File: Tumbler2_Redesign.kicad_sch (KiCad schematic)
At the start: 0 parts

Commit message: Add ESP32 and USB
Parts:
- added J1: USB_C_Receptacle_USB2.0_16P, symbol Connector:USB_C_Receptacle_USB2.0_16P
- added U1: ESP32-S3-WROOM-1, RF_Module:ESP32-S3-WROOM-1, symbol RF_Module:ESP32-S3-WROOM-1
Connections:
- new net: U1.1 (GND), U1.40 (GND), U1.41 (GND)
- new net: J1.A1 (GND), J1.A12 (GND), J1.B1 (GND), J1.B12 (GND)
- new net: J1.A4 (VBUS), J1.A9 (VBUS), J1.B4 (VBUS), J1.B9 (VBUS)
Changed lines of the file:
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@@
 	(generator_version "9.0")
 	(paper "A4")
+	(symbol
+		(lib_id "RF_Module:ESP32-S3-WROOM-1")
+		(at 142.24 86.36 0)
+		(unit 1)
+		(exclude_from_sim no)
+		(in_bom yes)
+		(on_board yes)
+		(dnp no)
+		(fields_autoplaced yes)
+		(property "Reference" "U1"
+			(at 144.3833 55.88 0)
+			(effects
+				(font
+					(size 1.27 1.27)
+				)
+				(justify left)
+			)
+		)
+		(property "Value" "ESP32-S3-WROOM-1"
+			(at 144.3833 58.42 0)
+			(effects
+				(font
+					(size 1.27 1.27)
+				)
+				(justify left)
+			)
+		)
+		(property "Footprint" "RF_Module:ESP32-S3-WROOM-1"
+			(at 142.24 83.82 0)
+			(effects
+				(font
+					(size 1.27 1.27)
+				)
+				(hide yes)
+			)
+		)
+		(property "Datasheet" "https://www.espressif.com/sites/default/files/documentation/esp32-s3-wroom-1_wroom-1u_datasheet_en.pdf"
+			(at 142.24 86.36 0)
+			(effects
+				(font
+					(size 1.27 1.27)
+				)
+				(hide yes)
+			)
+		)
+		(property "Description" "RF Module, ESP32-S3 SoC, Wi-Fi 802.11b/g/n, Bluetooth, BLE, 32-bit, 3.3V, onboard antenna, SMD"
+			(at 142.24 86.36 0)
+			(effects
+				(font
+					(size 1.27 1.27)
+				)
+				(hide yes)
+			)
+		)
+		(pin "12"
+		)
+		(pin "40"
+		)
+		(pin "20"
+		)
+		(pin "18"
+		)
+		(pin "15"
+		)
+		(pin "13"
+		)
+		(pin "23"
+		)
+		(pin "29"
+		)
+		(pin "31"
+		)
+		(pin "39"
+		)
+		(pin "3"
+		)
+		(pin "5"
+		)
+		(pin "17"
+		)
+		(pin "38"
+		)
+		(pin "19"
+		)
+		(pin "37"
+		)
+		(pin "27"
+		)
+		(pin "6"
+		)
+		(pin "8"
+		)
+		(pin "4"
+		)
+		(pin "7"
+		)
+		(pin "9"
+		)
+		(pin "2"
+		)
+		(pin "1"
+		)
+		(pin "22"
+		)
+		(pin "21"
+		)
+		(pin "41"
+		)
+		(pin "36"
+		)
+		(pin "10"
+		)
+		(pin "11"
+		)
+		(pin "14"
+		)
+		(pin "28"
+		)
+		(pin "30"
+		)
+		(pin "24"
+		)
+		(pin "33"
+		)
+		(pin "16"
+		)
+		(pin "26"
+		)
+		(pin "34"
+		)
+		(pin "25"
+		)
+		(pin "32"
+		)
+		(pin "35"
+		)
+		(instances
+			(project ""
+				(path "/f3fd8d79-9d35-4c04-811e-2697a2740958"
+					(reference "U1")
+					(unit 1)
+				)
+			)
+		)
+	)
+	(symbol
+		(lib_id "Connector:USB_C_Receptacle_USB2.0_16P")
+		(at 207.01 111.76 0)
+		(unit 1)
+		(exclude_from_sim no)
+		(in_bom yes)
+		(on_board yes)
+		(dnp no)
+		(fields_autoplaced yes)
+		(property "Reference" "J1"
+			(at 207.01 88.9 0)
+			(effects
+				(font
+					(size 1.27 1.27)
+				)
+			)
+		)
+		(property "Value" "USB_C_Receptacle_USB2.0_16P"
+			(at 207.01 91.44 0)
+			(effects
+				(font
+					(size 1.27 1.27)
+				)
+			)
+		)
+		(property "Footprint" ""
+			(at 210.82 111.76 0)
+			(effects
+				(font
+					(size 1.27 1.27)
+				)
+				(hide yes)
+			)
+		)
+		(property "Datasheet" "https://www.usb.org/sites/default/files/documents/usb_type-c.zip"
+			(at 210.82 111.76 0)
+			(effects
+				(font
+					(size 1.27 1.27)
+				)
+				(hide yes)
+			)
+		)
+		(property "Description" "USB 2.0-only 16P Type-C Receptacle connector"
+			(at 207.01 111.76 0)
+			(effects
+				(font
+					(size 1.27 1.27)
+				)
+				(hide yes)
+			)
+		)
+		(pin "S1"
+		)
+		(pin "B12"
+		)
+		(pin "B4"
+		)
+		(pin "A5"
+		)
+		(pin "A1"
+		)
+		(pin "A12"
+		)
+		(pin "B1"
+		)
+		(pin "A4"
+		)
+		(pin "A9"
+		)
+		(pin "B9"
+		)
+		(pin "B5"
+		)
+		(pin "B8"
+		)
+		(pin "A7"
+		)
+		(pin "B6"
+		)
+		(pin "B7"
+		)
+		(pin "A8"
+		)
+		(pin "A6"
+		)
+		(instances
+			(project ""
+				(path "/f3fd8d79-9d35-4c04-811e-2697a2740958"
+					(reference "J1")
+					(unit 1)
+				)
+			)
+		)
+	)
 	(sheet_instances
 		(path "/"

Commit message: Add further parts
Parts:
- added C1, C2, C3: C, symbol Device:C
- added D1: LED, symbol Device:LED
- added D2, D3, D4, D5: WS2812B, LED_SMD:LED_WS2812B-2020_PLCC4_2.0x2.0mm, symbol LED:WS2812B-2020
- added J2, J3: Conn_01x06, symbol Connector_Generic:Conn_01x06
- added J4, J5: Conn_01x04, symbol Connector_Generic:Conn_01x04
- added R1, R4, R5: R, symbol Device:R
- added R2, R3: 5k, symbol Device:R
- added SW1, SW2, SW3: SW_Push, symbol Switch:SW_Push
- added U2: USBLC6-2SC6, Package_TO_SOT_SMD:SOT-23-6, symbol Power_Protection:USBLC6-2SC6
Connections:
- net VBUS: now reaches J1.A4 (VBUS), J1.A9 (VBUS), J1.B4 (VBUS), J1.B9 (VBUS)
- net VBUS: now also U2.5 (VBUS)
- net at J1.A5 (CC1): now also R2.1
- net at J1.A6 (D+): now also J1.B6 (D+), U2.3 (I/O2)
- net at J1.A7 (D-): now also J1.B7 (D-), U2.1 (I/O1)
- net at J1.B5 (CC2): now also R3.1
- new net: D3.1 (DOUT), D4.3 (DIN)
- new net: D2.1 (DOUT), D3.3 (DIN)
- new net: D1.2 (A), R1.2
- new net: D4.1 (DOUT), D5.3 (DIN)
- new net GND: U2.2 (GND)

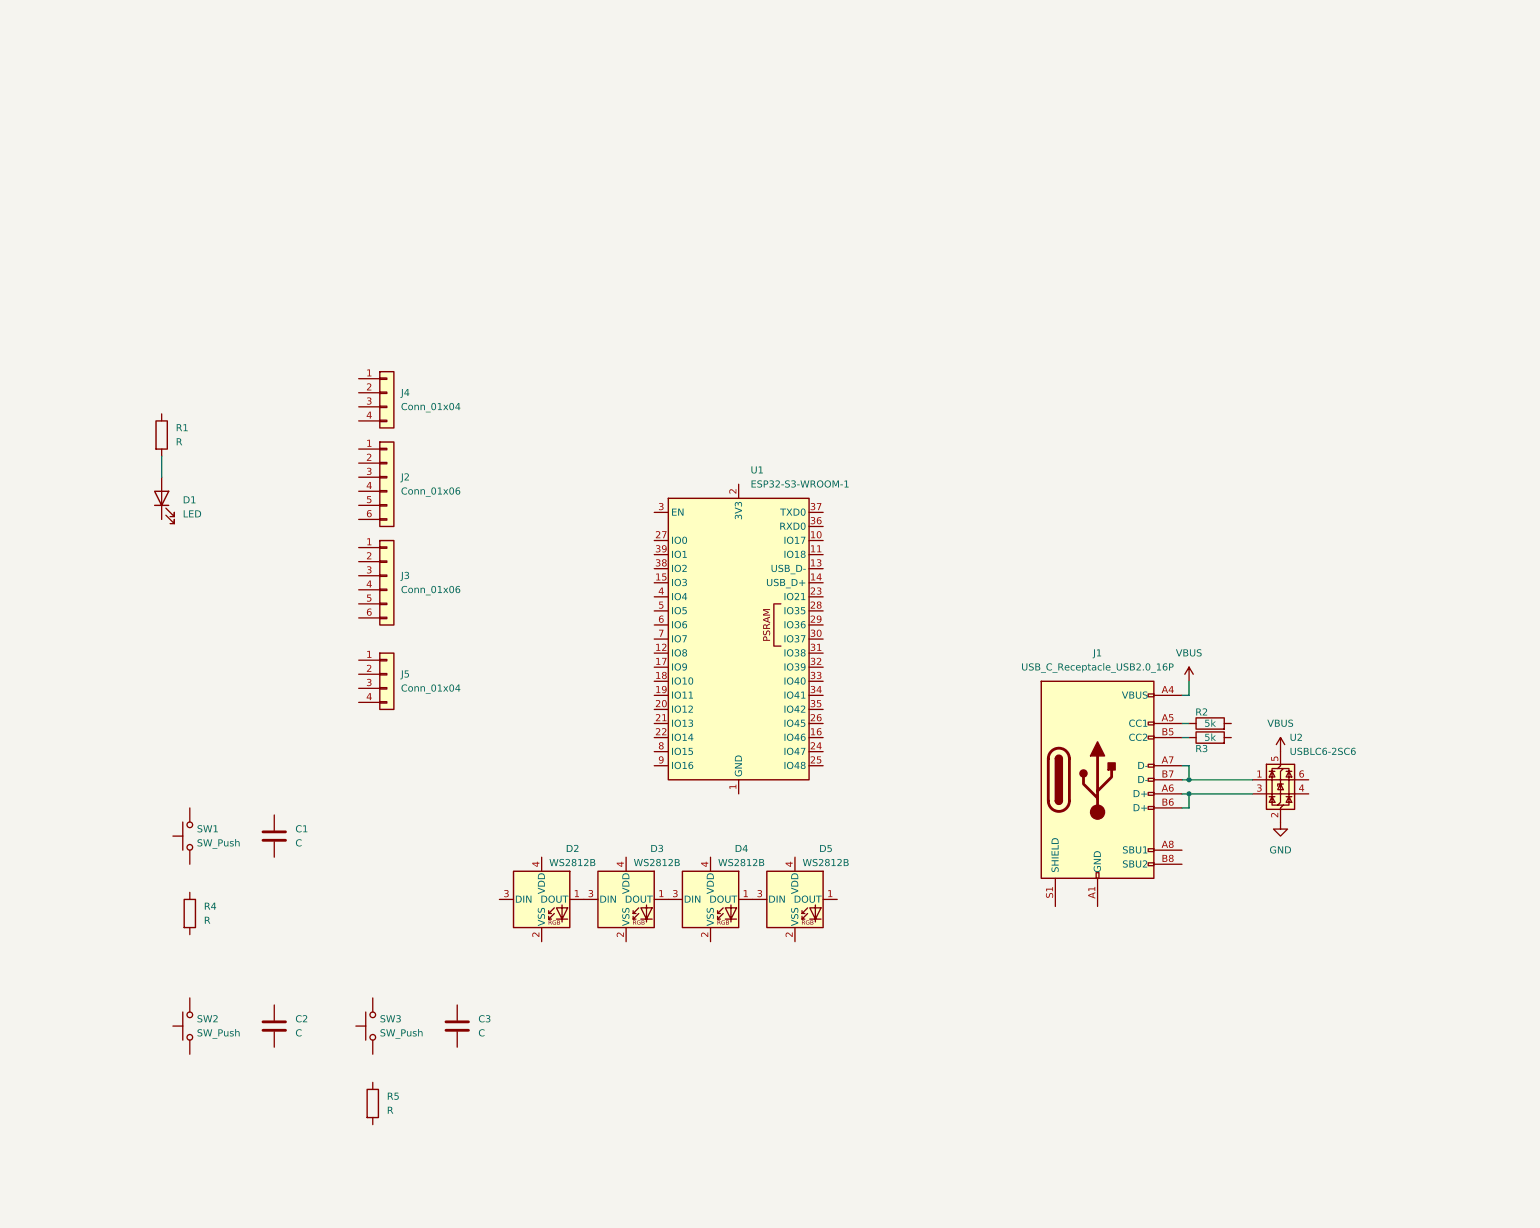
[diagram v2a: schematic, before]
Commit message: Add regulators and USB to UART
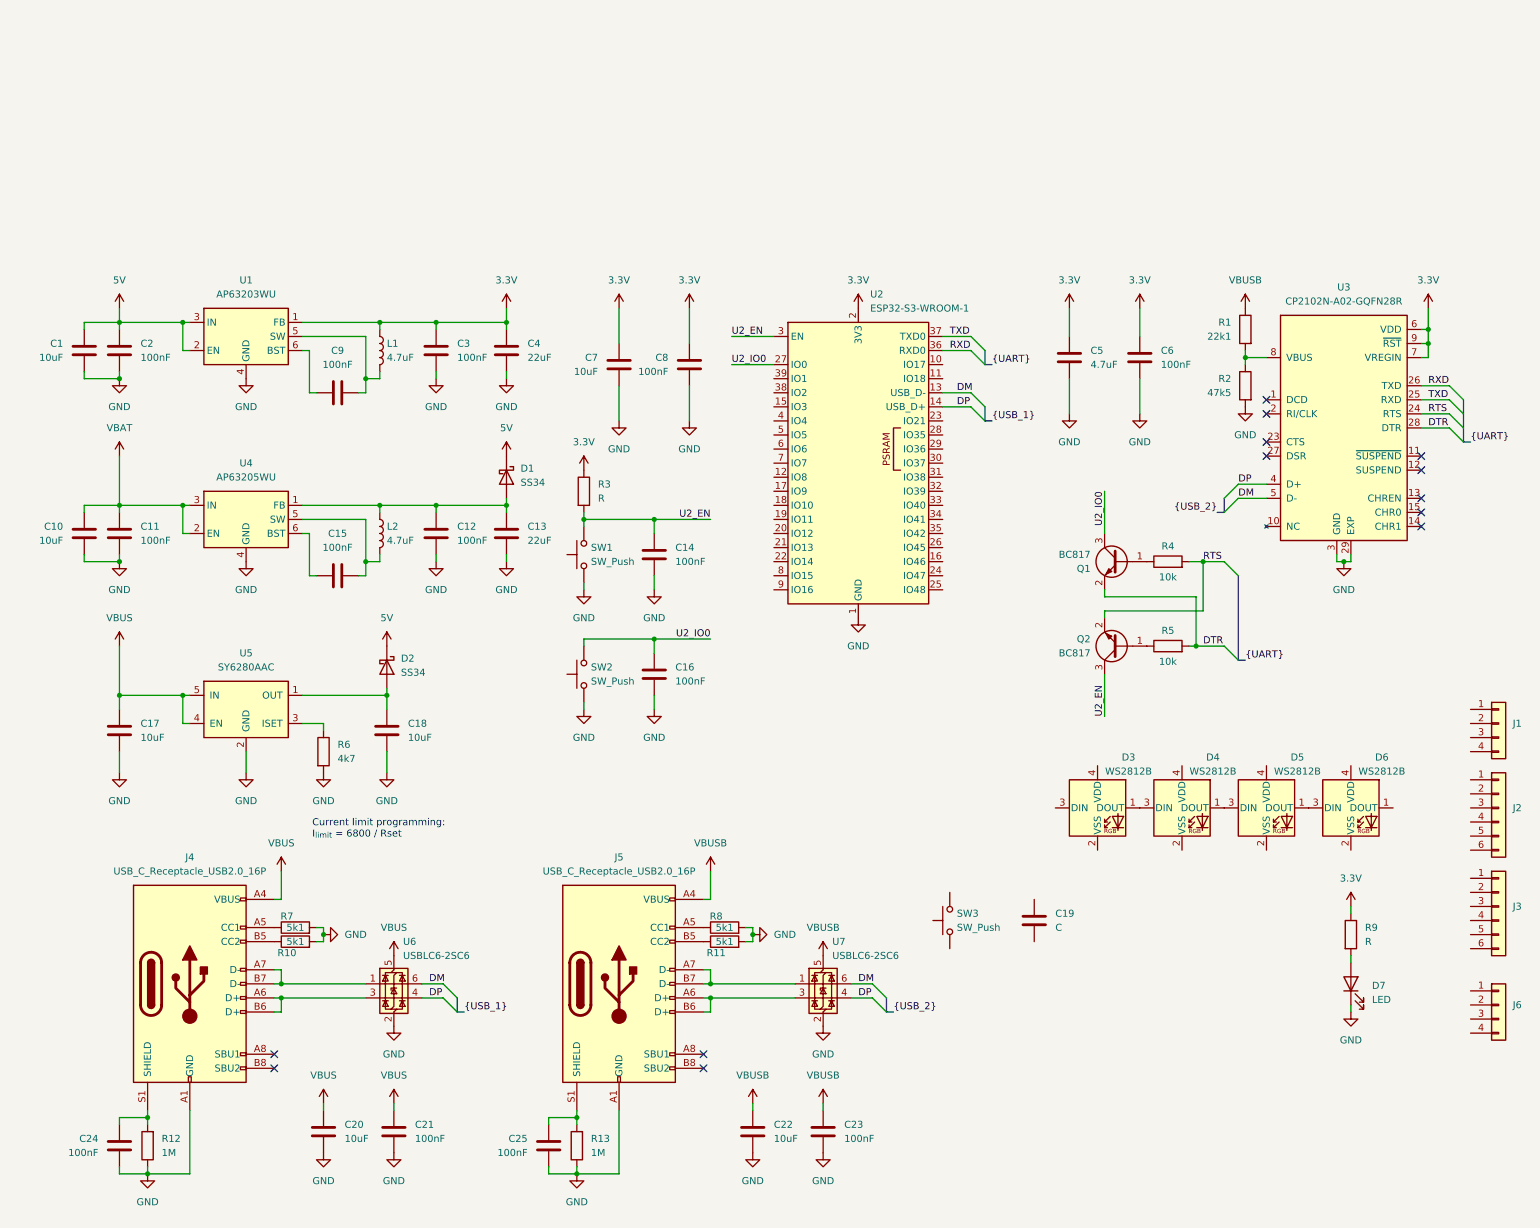
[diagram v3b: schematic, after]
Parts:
- removed SW3: SW_Push, symbol Switch:SW_Push
- added C1, C10, C17, C18, C20, C22, C7: 10uF, symbol Device:C
- added C11, C12, C15, C16, C2, C21, C23, C24, C25, C6, C8, C9: 100nF, symbol Device:C
- added C13, C4: 22uF, symbol Device:C
- added C5: 4.7uF, symbol Device:C
- added D1, D2: SS34, Diode_SMD:D_SMA, symbol Diode:SS34
- added J5: USB_C_Receptacle_USB2.0_16P, symbol Connector:USB_C_Receptacle_USB2.0_16P
- added L1, L2: 4.7uF, symbol Device:L
- added Q1, Q2: BC817, Package_TO_SOT_SMD:SOT-23, symbol Transistor_BJT:BC817
- added R1: 22k1, symbol Device:R
- added R11, R8: 5k1, symbol Device:R
- added R12, R13: 1M, symbol Device:R
- added R2: 47k5, symbol Device:R
- added R3: R, symbol Device:R
- added R6: 4k7, symbol Device:R
- added SW2: SW_Push, symbol Switch:SW_Push
- added U1: AP63203WU, Package_TO_SOT_SMD:TSOT-23-6, symbol Regulator_Switching:AP63203WU
- added U3: CP2102N-A02-GQFN28R, Package_DFN_QFN:QFN-28-1EP_5x5mm_P0.5mm_EP3.35x3.35mm, symbol Tumbler2:CP2102N-A02-GQFN28R
- added U4: AP63205WU, Package_TO_SOT_SMD:TSOT-23-6, symbol Regulator_Switching:AP63205WU
- added U5: SY6280AAC, Tumbler2:SOT95P285X130-5N, symbol Tumbler2:SY6280AAC
- added U7: USBLC6-2SC6, Package_TO_SOT_SMD:SOT-23-6, symbol Power_Protection:USBLC6-2SC6
- C14: renamed from C1; value C -> 100nF
- C3: value C -> 100nF
- R10: renamed from R3; value 5k -> 5k1
- R4, R5: value R -> 10k
- R7: renamed from R2; value 5k -> 5k1
- renumbered C2 to C19, D2 to D3, D3 to D4, D4 to D5, D5 to D6, D1 to D7, J4 to J1, J1 to J4, J5 to J6, R1 to R9, SW2 to SW3, U1 to U2, U2 to U6
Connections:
- net GND: now also C14.2, C3.2, D7.1 (K), J4.A1 (GND), J4.A12 (GND), J4.B1 (GND), J4.B12 (GND), R10.2, R7.2, SW1.1, U2.1 (GND), U2.40 (GND), U2.41 (GND), C1.2, C10.2, C11.2, C12.2, C13.2, C16.2, C17.2, C18.2, C2.2, C20.2, C21.2, C22.2, C23.2, C24.2, C25.2, C4.2, C5.2, C6.2, C7.2, C8.2, J5.A1 (GND), J5.A12 (GND), J5.B1 (GND), J5.B12 (GND), R11.2, R12.1, R13.1, R2.2, R6.2, R8.2, SW2.1, U1.4 (GND), U3.29 (EXP), U3.3 (GND), U4.4 (GND), U5.2 (GND), U7.2 (GND)
- net VBUS: now also C17.1, C20.1, C21.1, U5.4 (EN), U5.5 (IN)
- net DM: now reaches U2.13 (USB_D-)
- net DM: now also U6.6 (I/O1), U3.5 (D-), U7.6 (I/O1)
- net DP: now reaches U2.14 (USB_D+)
- net DP: now also U6.4 (I/O2), U3.4 (D+), U7.4 (I/O2)
- net 3.3V: now reaches U2.2 (3V3)
- net 3.3V: now also C3.1, R9.1, C4.1, C5.1, C6.1, C7.1, C8.1, L1.1, R3.1, U1.1 (FB), U3.6 (VDD), U3.7 (VREGIN), U3.9 (~{RST})
- net U2_IO0: now reaches U2.27 (IO0)
- net U2_IO0: now also C16.1, Q1.3 (C), SW2.2
- net U2_EN: now reaches U2.3 (EN)
- net U2_EN: now also C14.1, SW1.2, Q2.3 (C), R3.2
- net RXD: now reaches U2.36 (RXD0)
- net RXD: now also U3.26 (TXD)
- net TXD: now reaches U2.37 (TXD0)
- net TXD: now also U3.25 (RXD)
- net at R5.1: now also Q2.1 (B)
- net DTR: now reaches R5.2
- net DTR: now also Q1.2 (E), U3.28 (DTR)
- net at J4.S1 (SHIELD): now also C24.1, R12.2
- net at R4.1: now also Q1.1 (B)
- net RTS: now reaches R4.2
- net RTS: now also Q2.2 (E), U3.24 (RTS)
- new net: C9.1, L1.2, U1.5 (SW)
- new net: C9.2, U1.6 (BST)
- new net: R1.2, R2.1, U3.8 (VBUS)
- new net: C12.1, C13.1, D1.2 (A), L2.1, U4.1 (FB)
- new net: C15.1, L2.2, U4.5 (SW)
- new net: R6.1, U5.3 (ISET)
- new net: J5.A5 (CC1), R8.1
- new net: C25.1, J5.S1 (SHIELD), R13.2
- new net: J5.A6 (D+), J5.B6 (D+), U7.3 (I/O2)
- new net: J5.A7 (D-), J5.B7 (D-), U7.1 (I/O1)
- new net: J5.B5 (CC2), R11.1
- new net: C18.1, D2.2 (A), U5.1 (OUT)
- new net: C15.2, U4.6 (BST)
- new net: U3.16 (GPIO3_WAKEUP), U3.17 (GPIO2_RS485), U3.18 (GPIO1_RXT), U3.19 (GPIO0_TXT), U3.20 (GPIO6), U3.21 (GPIO5), U3.22 (GPIO4)
- new net 5V: C1.1, C2.1, D1.1 (K), D2.1 (K), U1.2 (EN), U1.3 (IN)
- new net VBAT: C10.1, C11.1, U4.2 (EN), U4.3 (IN)
- new net VBUSB: C22.1, C23.1, J5.A4 (VBUS), J5.A9 (VBUS), J5.B4 (VBUS), J5.B9 (VBUS), R1.1, U7.5 (VBUS)
- no-connect marks 0 -> 13
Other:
- note added: "Current limit programming: I_{limit} = 6800 / Rset"
- moved on the sheet: C14, C19, D3, D4, D5, D6, D7, J1, J2, J3, J4, J6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

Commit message: Remove overcurrent protection
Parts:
- removed C17, C18: 10uF, symbol Device:C
- removed D2: SS34, Diode_SMD:D_SMA, symbol Diode:SS34
- removed R6: 4k7, symbol Device:R
- removed U5: SY6280AAC, Tumbler2:SOT95P285X130-5N, symbol Tumbler2:SY6280AAC
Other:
- note added: "Battery Charging IC INJOINIC IP5306 TI BQ25887RGER"
- note removed: "Current limit programming: I_{limit} = 6800 / Rset"
